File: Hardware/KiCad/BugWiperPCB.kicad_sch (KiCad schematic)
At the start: 10 parts, among them J2 TBLH10-350-06BK, J3 Phoenix_1776508

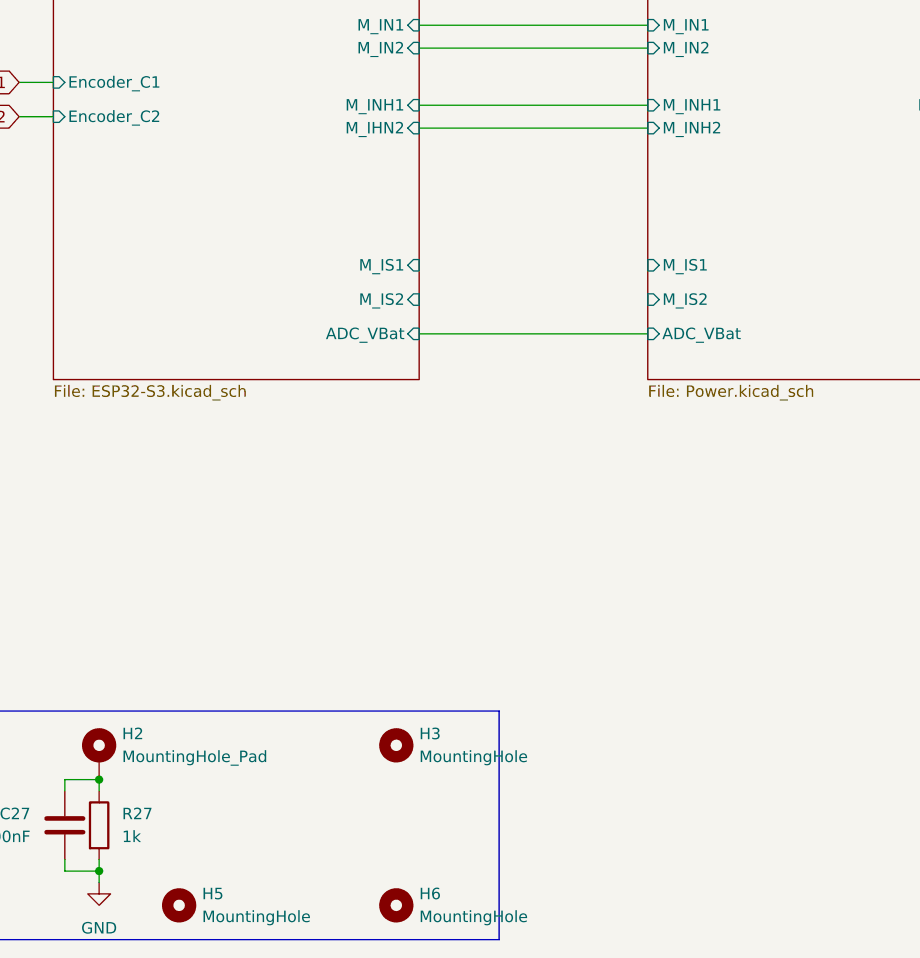
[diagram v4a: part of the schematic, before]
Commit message: add debug connector, arrange foodprints and add NTC and connect to GPIOs to ESP32
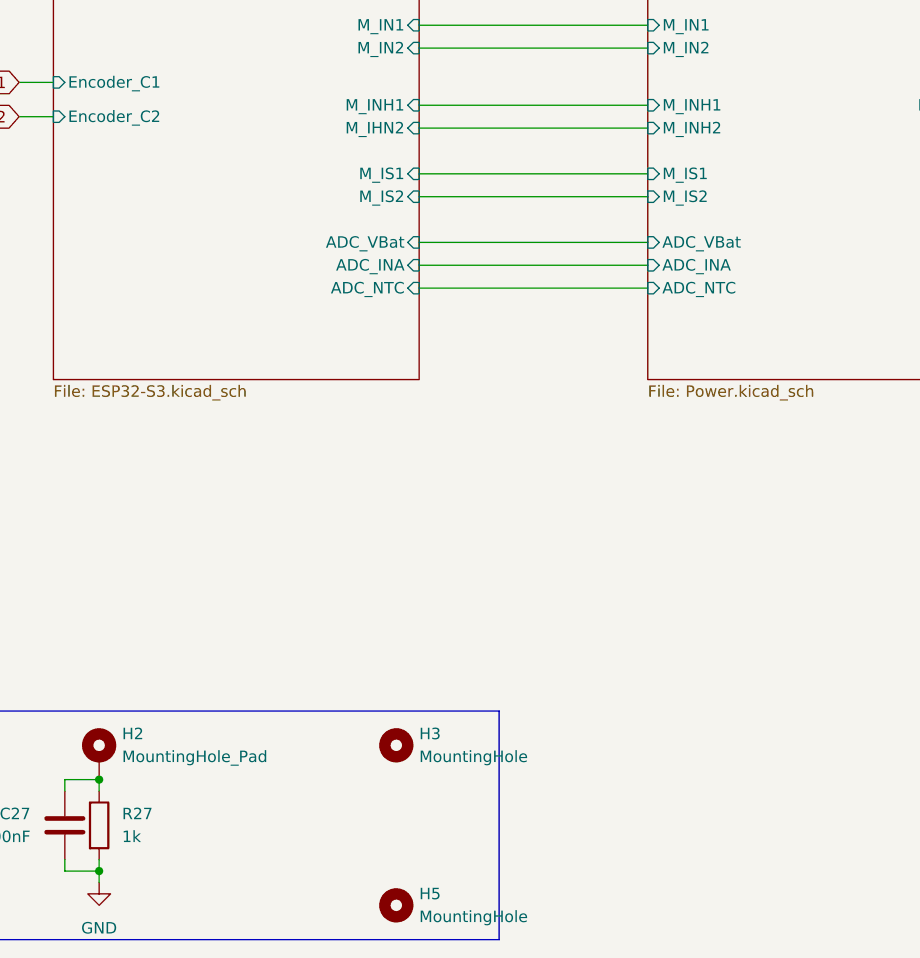
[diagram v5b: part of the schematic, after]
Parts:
- removed H5: MountingHole, MountingHole:MountingHole_3.2mm_M3_DIN965, symbol Mechanical:MountingHole
- renumbered H6 to H5
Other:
- sheet ESP32-S3 ports: added ADC_INA, ADC_NTC; removed none
- sheet Power ports: added ADC_INA, ADC_NTC; removed none
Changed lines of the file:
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@@
+    (stroke (width 0) (type default))
+  )
+  (wire (pts (xy 116.84 81.28) (xy 142.24 81.28))
     (stroke (width 0) (type default))
   )
@@
     (stroke (width 0) (type default))
   )
+  (wire (pts (xy 116.84 93.98) (xy 142.24 93.98))
+    (stroke (width 0) (type default))
+  )
   (wire (pts (xy 81.28 158.75) (xy 81.28 160.02))
     (stroke (width 0) (type default))
@@
     (stroke (width 0) (type default))
   )
-  (wire (pts (xy 116.84 99.06) (xy 142.24 99.06))
+  (wire (pts (xy 116.84 88.9) (xy 142.24 88.9))
     (stroke (width 0) (type default))
   )
@@
     (stroke (width 0) (type default))
   )
+  (wire (pts (xy 116.84 91.44) (xy 142.24 91.44))
+    (stroke (width 0) (type default))
+  )
   (wire (pts (xy 116.84 73.66) (xy 142.24 73.66))
     (stroke (width 0) (type default))
@@
   )
   (wire (pts (xy 77.47 158.75) (xy 81.28 158.75))
+    (stroke (width 0) (type default))
+  )
+  (wire (pts (xy 116.84 83.82) (xy 142.24 83.82))
     (stroke (width 0) (type default))
   )
@@
         (path "/d31a15bd-db02-4d4c-9593-17c596d3182c"
           (reference "C27") (unit 1)
-        )
-      )
-    )
-  )
-  (symbol (lib_id "Mechanical:MountingHole") (at 90.17 162.56 0) (unit 1)
-    (in_bom yes) (on_board yes) (dnp no) (fields_autoplaced)
-    (property "Reference" "H5" (at 92.71 161.29 0)
-      (effects (font (size 1.27 1.27)) (justify left))
-    )
-    (property "Value" "MountingHole" (at 92.71 163.83 0)
-      (effects (font (size 1.27 1.27)) (justify left))
-    )
-    (property "Footprint" "MountingHole:MountingHole_3.2mm_M3_DIN965" (at 90.17 162.56 0)
-      (effects (font (size 1.27 1.27)) hide)
-    )
-    (property "Datasheet" "~" (at 90.17 162.56 0)
-      (effects (font (size 1.27 1.27)) hide)
-    )
-    (instances
-      (project "BugWiperPCB"
-        (path "/d31a15bd-db02-4d4c-9593-17c596d3182c"
-          (reference "H5") (unit 1)
         )
       )
@@
   (symbol (lib_id "Mechanical:MountingHole") (at 114.3 162.56 0) (unit 1)
     (in_bom yes) (on_board yes) (dnp no) (fields_autoplaced)
-    (property "Reference" "H6" (at 116.84 161.29 0)
+    (property "Reference" "H5" (at 116.84 161.29 0)
       (effects (font (size 1.27 1.27)) (justify left))
     )
@@
       (project "BugWiperPCB"
         (path "/d31a15bd-db02-4d4c-9593-17c596d3182c"
-          (reference "H6") (unit 1)
+          (reference "H5") (unit 1)
         )
       )
@@
       (effects (font (size 1.27 1.27)) (justify right))
     )
-    (pin "ADC_VBat" input (at 142.24 99.06 180)
+    (pin "ADC_VBat" input (at 142.24 88.9 180)
       (effects (font (size 1.27 1.27)) (justify left))
     )
@@
       (effects (font (size 1.27 1.27)) (justify left))
     )
-    (pin "M_IS2" input (at 142.24 95.25 180)
-      (effects (font (size 1.27 1.27)) (justify left))
-    )
-    (pin "M_IS1" input (at 142.24 91.44 180)
+    (pin "M_IS2" input (at 142.24 83.82 180)
+      (effects (font (size 1.27 1.27)) (justify left))
+    )
+    (pin "M_IS1" input (at 142.24 81.28 180)
       (effects (font (size 1.27 1.27)) (justify left))
     )
@@
     )
     (pin "GND" input (at 142.24 54.61 180)
+      (effects (font (size 1.27 1.27)) (justify left))
+    )
+    (pin "ADC_INA" input (at 142.24 91.44 180)
+      (effects (font (size 1.27 1.27)) (justify left))
+    )
+    (pin "ADC_NTC" input (at 142.24 93.98 180)
       (effects (font (size 1.27 1.27)) (justify left))
     )
@@
       (effects (font (size 1.27 1.27)) (justify left))
     )
-    (pin "ADC_VBat" input (at 116.84 99.06 0)
-      (effects (font (size 1.27 1.27)) (justify right))
-    )
-    (pin "M_IS2" input (at 116.84 95.25 0)
-      (effects (font (size 1.27 1.27)) (justify right))
-    )
-    (pin "M_IS1" input (at 116.84 91.44 0)
+    (pin "ADC_VBat" input (at 116.84 88.9 0)
+      (effects (font (size 1.27 1.27)) (justify right))
+    )
+    (pin "M_IS2" input (at 116.84 83.82 0)
+      (effects (font (size 1.27 1.27)) (justify right))
+    )
+    (pin "M_IS1" input (at 116.84 81.28 0)
       (effects (font (size 1.27 1.27)) (justify right))
     )
@@
       (effects (font (size 1.27 1.27)) (justify right))
     )
+    (pin "ADC_INA" input (at 116.84 91.44 0)
+      (effects (font (size 1.27 1.27)) (justify right))
+    )
+    (pin "ADC_NTC" input (at 116.84 93.98 0)
+      (effects (font (size 1.27 1.27)) (justify right))
+    )

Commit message: add resistor arrays
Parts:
- added F2: 10mA Polyfuse, Resistor_SMD:R_1206_3216Metric, symbol Device:Polyfuse
- added JP2: SolderJumper_3_Open, BugWiper_lib:SolderJumper_R_SMD_0603, symbol Jumper:SolderJumper_3_Bridged12
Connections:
- net +3V3: no longer names the net of J2.3_A (3), J2.3_B (3__1)
- net +3V3: now also F2.1
- new net: F2.2, JP2.2 (C)
- new net +12V: JP2.3 (B)
- new net +3.3V: JP2.1 (A)
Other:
- sheet Power ports: added +12V; removed none
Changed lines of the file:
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@@
   (junction (at 231.14 139.7) (diameter 0) (color 0 0 0 0)
   )
+  (junction (at 128.27 50.8) (diameter 0) (color 0 0 0 0)
+  )
   (junction (at 231.14 144.78) (diameter 0) (color 0 0 0 0)
   )
@@
   (junction (at 231.14 152.4) (diameter 0) (color 0 0 0 0)
   )
+  (wire (pts (xy 207.01 132.08) (xy 207.01 134.62))
+    (stroke (width 0) (type default))
+  )
   (wire (pts (xy 226.06 152.4) (xy 231.14 152.4))
     (stroke (width 0) (type default))
@@
     (stroke (width 0) (type default))
   )
-  (wire (pts (xy 224.79 139.7) (xy 231.14 139.7))
+  (wire (pts (xy 207.01 147.32) (xy 207.01 144.78))
     (stroke (width 0) (type default))
   )
@@
     (stroke (width 0) (type default))
   )
+  (wire (pts (xy 198.12 147.32) (xy 207.01 147.32))
+    (stroke (width 0) (type default))
+  )
   (wire (pts (xy 224.79 129.54) (xy 231.14 129.54))
     (stroke (width 0) (type default))
@@
     (stroke (width 0) (type default))
   )
+  (wire (pts (xy 180.34 67.31) (xy 187.96 67.31))
+    (stroke (width 0) (type default))
+  )
   (wire (pts (xy 77.47 158.75) (xy 77.47 157.48))
     (stroke (width 0) (type default))
@@
     (stroke (width 0) (type default))
   )
+  (wire (pts (xy 196.85 132.08) (xy 207.01 132.08))
+    (stroke (width 0) (type default))
+  )
   (wire (pts (xy 72.39 74.93) (xy 76.2 74.93))
     (stroke (width 0) (type default))
@@
     (stroke (width 0) (type default))
   )
+  (wire (pts (xy 128.27 49.53) (xy 128.27 50.8))
+    (stroke (width 0) (type default))
+  )
   (wire (pts (xy 231.14 134.62) (xy 231.14 137.16))
     (stroke (width 0) (type default))
   )
+  (wire (pts (xy 210.82 139.7) (xy 215.9 139.7))
+    (stroke (width 0) (type default))
+  )
+  (wire (pts (xy 128.27 50.8) (xy 142.24 50.8))
+    (stroke (width 0) (type default))
+  )
   (wire (pts (xy 116.84 91.44) (xy 142.24 91.44))
     (stroke (width 0) (type default))
   )
+  (wire (pts (xy 223.52 139.7) (xy 231.14 139.7))
+    (stroke (width 0) (type default))
+  )
   (wire (pts (xy 116.84 73.66) (xy 142.24 73.66))
     (stroke (width 0) (type default))
   )
-  (wire (pts (xy 116.84 50.8) (xy 142.24 50.8))
+  (wire (pts (xy 116.84 50.8) (xy 128.27 50.8))
     (stroke (width 0) (type default))
   )
@@
     )
   )
-  (global_label "+3V3" (shape input) (at 224.79 139.7 180) (fields_autoplaced)
-    (effects (font (size 1.27 1.27)) (justify right))
-    (property "Intersheetrefs" "${INTERSHEET_REFS}" (at 216.7248 139.7 0)
-      (effects (font (size 1.27 1.27)) (justify right) hide)
-    )
-  )
   (global_label "Motor+" (shape input) (at 224.79 129.54 180) (fields_autoplaced)
     (effects (font (size 1.27 1.27)) (justify right))
@@
     )
   )
+  (symbol (lib_id "power:+3.3V") (at 196.85 132.08 90) (unit 1)
+    (in_bom yes) (on_board yes) (dnp no) (fields_autoplaced)
+    (property "Reference" "#PWR065" (at 200.66 132.08 0)
+      (effects (font (size 1.27 1.27)) hide)
+    )
+    (property "Value" "+3.3V" (at 193.04 132.08 90)
+      (effects (font (size 1.27 1.27)) (justify left))
+    )
+    (property "Footprint" "" (at 196.85 132.08 0)
+      (effects (font (size 1.27 1.27)) hide)
+    )
+    (property "Datasheet" "" (at 196.85 132.08 0)
+      (effects (font (size 1.27 1.27)) hide)
+    )
+    (pin "1")
+    (instances
+      (project "BugWiperPCB"
+        (path "/d31a15bd-db02-4d4c-9593-17c596d3182c"
+          (reference "#PWR065") (unit 1)
+        )
+      )
+    )
+  )
+  (symbol (lib_id "Jumper:SolderJumper_3_Bridged12") (at 207.01 139.7 90) (mirror x) (unit 1)
+    (in_bom yes) (on_board yes) (dnp no) (fields_autoplaced)
+    (property "Reference" "JP2" (at 204.47 138.43 90)
+      (effects (font (size 1.27 1.27)) (justify left))
+    )
+    (property "Value" "SolderJumper_3_Open" (at 204.47 140.97 90)
+      (effects (font (size 1.27 1.27)) (justify left))
+    )
+    (property "Footprint" "BugWiper_lib:SolderJumper_R_SMD_0603" (at 207.01 139.7 0)
+      (effects (font (size 1.27 1.27)) hide)
+    )
+    (property "Datasheet" "~" (at 207.01 139.7 0)
+      (effects (font (size 1.27 1.27)) hide)
+    )
+    (pin "1")
+    (pin "3")
+    (pin "2")
+    (instances
+      (project "BugWiperPCB"
+        (path "/d31a15bd-db02-4d4c-9593-17c596d3182c"
+          (reference "JP2") (unit 1)
+        )
+      )
+    )
+  )
   (symbol (lib_id "BugWiper_Lib:Phoenix_1776508") (at 156.21 31.75 90) (unit 1)
     (in_bom yes) (on_board yes) (dnp no) (fields_autoplaced)
@@
     )
   )
+  (symbol (lib_id "Device:Polyfuse") (at 219.71 139.7 270) (unit 1)
+    (in_bom yes) (on_board yes) (dnp no)
+    (property "Reference" "F2" (at 218.44 137.16 90)
+      (effects (font (size 1.27 1.27)) (justify right))
+    )
+    (property "Value" "10mA Polyfuse" (at 227.33 142.24 90)
+      (effects (font (size 1.27 1.27)) (justify right))
+    )
+    (property "Footprint" "Resistor_SMD:R_1206_3216Metric" (at 214.63 140.97 0)
+      (effects (font (size 1.27 1.27)) (justify left) hide)
+    )
+    (property "Datasheet" "~" (at 219.71 139.7 0)
+      (effects (font (size 1.27 1.27)) hide)
+    )
+    (pin "1")
+    (pin "2")
+    (instances
+      (project "BugWiperPCB"
+        (path "/d31a15bd-db02-4d4c-9593-17c596d3182c"
+          (reference "F2") (unit 1)
+        )
+      )
+    )
+  )
+  (symbol (lib_id "power:+12V") (at 187.96 67.31 270) (unit 1)
+    (in_bom yes) (on_board yes) (dnp no) (fields_autoplaced)
+    (property "Reference" "#PWR063" (at 184.15 67.31 0)
+      (effects (font (size 1.27 1.27)) hide)
+    )
+    (property "Value" "+12V" (at 191.77 67.31 90)
+      (effects (font (size 1.27 1.27)) (justify left))
+    )
+    (property "Footprint" "" (at 187.96 67.31 0)
+      (effects (font (size 1.27 1.27)) hide)
+    )
+    (property "Datasheet" "" (at 187.96 67.31 0)
+      (effects (font (size 1.27 1.27)) hide)
+    )
+    (pin "1")
+    (instances
+      (project "BugWiperPCB"
+        (path "/d31a15bd-db02-4d4c-9593-17c596d3182c"
+          (reference "#PWR063") (unit 1)
+        )
+      )
+    )
+  )
   (symbol (lib_id "Mechanical:MountingHole") (at 114.3 144.78 0) (unit 1)
     (in_bom yes) (on_board yes) (dnp no) (fields_autoplaced)
@@
         (path "/d31a15bd-db02-4d4c-9593-17c596d3182c"
           (reference "H3") (unit 1)
+        )
+      )
+    )
+  )
+  (symbol (lib_id "power:+12V") (at 198.12 147.32 90) (unit 1)
+    (in_bom yes) (on_board yes) (dnp no) (fields_autoplaced)
+    (property "Reference" "#PWR064" (at 201.93 147.32 0)
+      (effects (font (size 1.27 1.27)) hide)
+    )
+    (property "Value" "+12V" (at 194.31 147.32 90)
+      (effects (font (size 1.27 1.27)) (justify left))
+    )
+    (property "Footprint" "" (at 198.12 147.32 0)
+      (effects (font (size 1.27 1.27)) hide)
+    )
+    (property "Datasheet" "" (at 198.12 147.32 0)
+      (effects (font (size 1.27 1.27)) hide)
+    )
+    (pin "1")
+    (instances
+      (project "BugWiperPCB"
+        (path "/d31a15bd-db02-4d4c-9593-17c596d3182c"
+          (reference "#PWR064") (unit 1)
         )
       )
@@
         (path "/d31a15bd-db02-4d4c-9593-17c596d3182c"
           (reference "H1") (unit 1)
+        )
+      )
+    )
+  )
+  (symbol (lib_id "power:+3.3V") (at 128.27 49.53 0) (unit 1)
+    (in_bom yes) (on_board yes) (dnp no) (fields_autoplaced)
+    (property "Reference" "#PWR062" (at 128.27 53.34 0)
+      (effects (font (size 1.27 1.27)) hide)
+    )
+    (property "Value" "+3.3V" (at 128.27 44.45 0)
+      (effects (font (size 1.27 1.27)))
+    )
+    (property "Footprint" "" (at 128.27 49.53 0)
+      (effects (font (size 1.27 1.27)) hide)
+    )
+    (property "Datasheet" "" (at 128.27 49.53 0)
+      (effects (font (size 1.27 1.27)) hide)
+    )
+    (pin "1")
+    (instances
+      (project "BugWiperPCB"
+        (path "/d31a15bd-db02-4d4c-9593-17c596d3182c"
+          (reference "#PWR062") (unit 1)
         )
       )
@@
       (effects (font (size 1.27 1.27)) (justify left))
     )
-    (instances
+    (pin "+12V" input (at 180.34 67.31 0)
+      (effects (font (size 1.27 1.27)) (justify right))
+    )
+    (instances
